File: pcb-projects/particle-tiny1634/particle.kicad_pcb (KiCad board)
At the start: 2 copper layers, 16 parts, among them IC1 ATTINY1634-SU, P1 CONN_02X03, P2 CONN_02X03

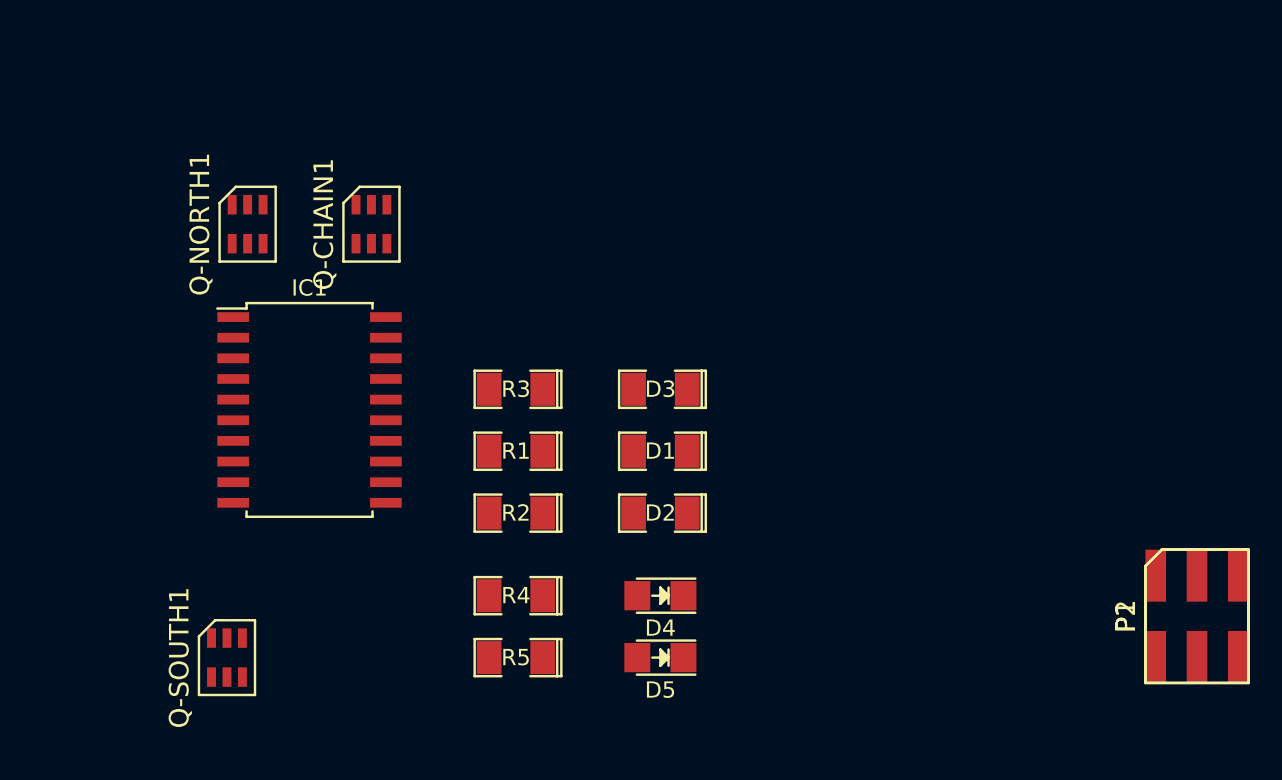
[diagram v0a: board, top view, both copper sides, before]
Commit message: routed attiny1634 particle
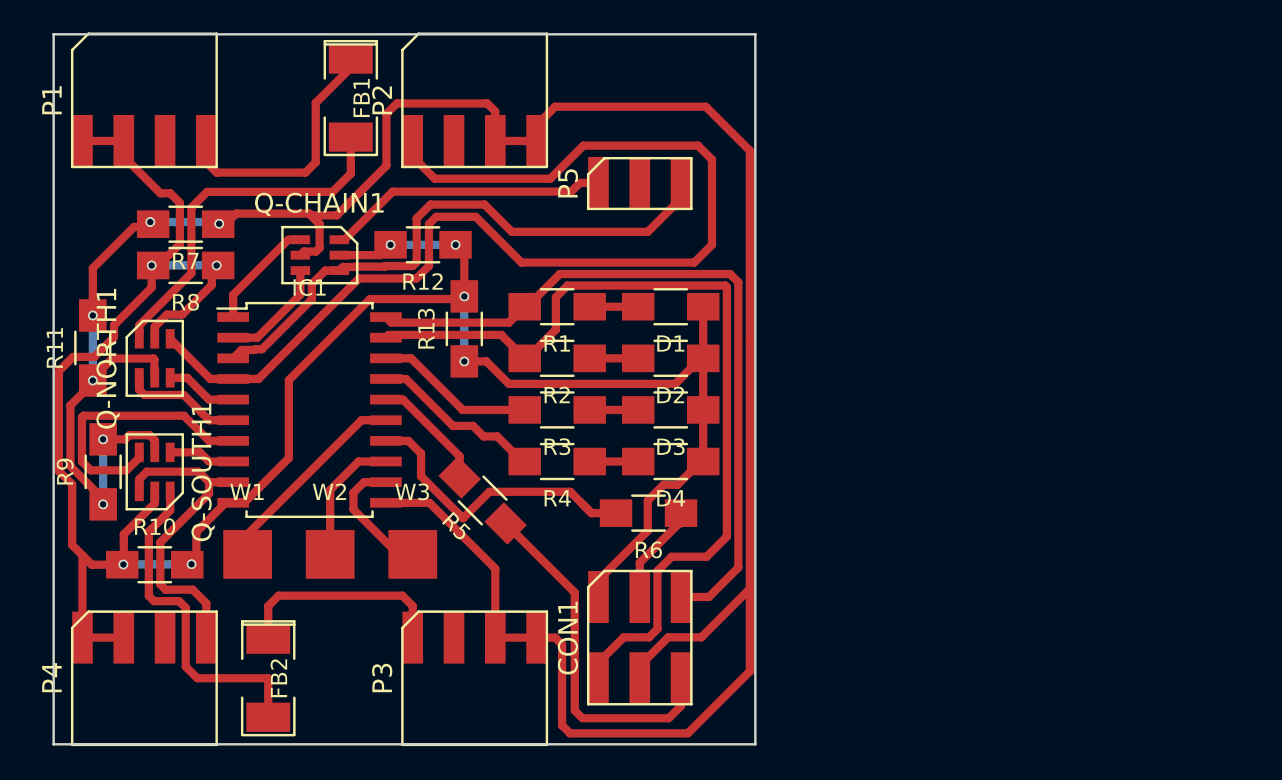
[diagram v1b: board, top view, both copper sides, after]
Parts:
- removed D5: LED, LEDs:LED-1206
- added CON1: AVR-ISP-6, SMT_PIN_HEADER:CONN-6, F.Cu at (170.2, 122.0)
- added FB1: TX-SMA-N, SMD_Packages:SMD-2010_Pol, F.Cu at (152.4, 88.8)
- added FB2: TX-SMA-S, SMD_Packages:SMD-2010_Pol, F.Cu at (147.3, 124.5)
- added P3: TXS, SMT_PIN_HEADER:CONN-8_5-8, F.Cu at (160.0, 124.5)
- added P4: RXS, SMT_PIN_HEADER:CONN-8_5-8, F.Cu at (139.7, 124.5)
- added P5: TRXCH, SMT_PIN_HEADER:CONN-1x3, F.Cu at (170.2, 94.0)
- added R10: 0, Resistors_SMD:R_1206_HandSoldering, F.Cu at (140.3, 117.5)
- added R11: 0, Resistors_SMD:R_1206_HandSoldering, F.Cu at (136.5, 104.1)
- added R12: 0, Resistors_SMD:R_1206_HandSoldering, F.Cu at (156.8, 97.8)
- added R13: 0, Resistors_SMD:R_1206_HandSoldering, F.Cu at (159.4, 103.0)
- added R6: 0, Resistors_SMD:R_1206_HandSoldering, F.Cu at (170.7, 114.3)
- added R7: 0, Resistors_SMD:R_1206_HandSoldering, F.Cu at (142.2, 96.5)
- added R8: 0, Resistors_SMD:R_1206_HandSoldering, F.Cu at (142.2, 99.1)
- added R9: 0, Resistors_SMD:R_1206_HandSoldering, F.Cu at (137.2, 111.8)
- added W1: TEST_1P, Measurement_Points:Measurement_Point_Square-SMD-Pad_Big, F.Cu at (146.1, 116.8)
- added W2: TEST_1P, Measurement_Points:Measurement_Point_Square-SMD-Pad_Big, F.Cu at (151.1, 116.8)
- added W3: TEST_1P, Measurement_Points:Measurement_Point_Square-SMD-Pad_Big, F.Cu at (156.2, 116.8)
- D1: value LED -> HB; footprint SMD_Packages:SMD-1206_Pol -> Resistors_SMD:R_1206_HandSoldering
- D2: value LED -> STATUS0; footprint SMD_Packages:SMD-1206_Pol -> Resistors_SMD:R_1206_HandSoldering
- D3: value LED -> STATUS1; footprint SMD_Packages:SMD-1206_Pol -> Resistors_SMD:R_1206_HandSoldering
- D4: value LED -> ERROR; footprint LEDs:LED-1206 -> Resistors_SMD:R_1206_HandSoldering
- P1: value CONN_02X03 -> TXN; footprint SMT_PIN_HEADER:CONN-6_1-3 -> SMT_PIN_HEADER:CONN-8_1-4
- P2: value CONN_02X03 -> RXN; footprint SMT_PIN_HEADER:CONN-6_4-6 -> SMT_PIN_HEADER:CONN-8_1-4
- R1, R2, R3, R4: value R_Small -> 1k2; footprint SMD_Packages:SMD-1206_Pol -> Resistors_SMD:R_1206_HandSoldering
- R5: value R_Small -> 0; footprint SMD_Packages:SMD-1206_Pol -> Resistors_SMD:R_1206_HandSoldering
- moved P1 72.1 mm to (139.7, 88.9)
- moved P2 54.6 mm to (160.0, 88.9)
- moved Q-SOUTH1 12.3 mm to (140.3, 111.8), turned to 180 degrees
- moved Q-NORTH1 10.0 mm to (140.3, 104.8)
- moved R5 9.88 mm to (160.5, 113.5), turned to 135 degrees
- moved R2 9.86 mm to (165.1, 104.8)
- moved D2 9.55 mm to (172.1, 104.8)
- moved R1 9.25 mm to (165.1, 101.6)
- moved D1 8.91 mm to (172.1, 101.6)
- moved R4 8.64 mm to (165.1, 111.1)
- moved D4 8.28 mm to (172.1, 111.1)
- moved Q-CHAIN1 3.70 mm to (150.5, 98.4), turned to 270 degrees
- moved R3 2.84 mm to (165.1, 108.0)
- moved D3 1.42 mm to (172.1, 108.0)
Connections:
- D1 pad 1: VCC -> GND
- D2 pad 1: VCC -> GND
- D3 pad 1: VCC -> GND
- D4 pad 1: VCC -> GND
- IC1 pad 1: (no net) -> /PWR/TX-CHAIN
- IC1 pad 10: (no net) -> GND
- IC1 pad 12: (no net) -> /TP3
- IC1 pad 13: (no net) -> /TP2
- IC1 pad 14: (no net) -> Net-(IC1-Pad14)
- IC1 pad 15: (no net) -> /TP1
- IC1 pad 16: (no net) -> Net-(IC1-Pad16)
- IC1 pad 17: (no net) -> /ERROR
- IC1 pad 18: (no net) -> /STATUS1
- IC1 pad 19: (no net) -> /MISO
- IC1 pad 2: (no net) -> /SW_PWR/RX-CHAIN
- IC1 pad 20: (no net) -> /MOSI
- IC1 pad 3: (no net) -> /RX-CHAIN
- IC1 pad 4: (no net) -> /RX-NORTH
- IC1 pad 5: (no net) -> /SW_PWR/RX-NORTH
- IC1 pad 6: (no net) -> /PWR/TX-NORTH
- IC1 pad 7: (no net) -> /SW_PWR/RX-SOUTH
- IC1 pad 8: (no net) -> /PWR/TX-SOUTH
- IC1 pad 9: (no net) -> /RX-SOUTH
- P1 pad 1: (no net) -> GND
- P1 pad 2: (no net) -> GND
- P2 pad 4: (no net) -> VCC
- Q-CHAIN1 pad 1: (no net) -> /PWR/TX-CHAIN
- Q-CHAIN1 pad 3: (no net) -> /SW_PWR/RX-CHAIN
- Q-CHAIN1 pad 4: (no net) -> /RX-CHAIN
- Q-NORTH1 pad 1: (no net) -> /PWR/TX-NORTH
- Q-NORTH1 pad 3: (no net) -> /SW_PWR/RX-NORTH
- Q-NORTH1 pad 4: (no net) -> /RX-NORTH
- Q-NORTH1 pad 6: /TX-NORTH -> Net-(FB1-Pad2)
- Q-SOUTH1 pad 1: (no net) -> /PWR/TX-SOUTH
- Q-SOUTH1 pad 3: (no net) -> /SW_PWR/RX-SOUTH
- Q-SOUTH1 pad 4: (no net) -> /RX-SOUTH
- Q-SOUTH1 pad 6: /TX-SOUTH -> Net-(FB2-Pad2)
- R1 pad 2: /TX-SOUTH -> /MOSI
- R2 pad 2: /TX-NORTH -> /MISO
- R3 pad 2: /TX-CHAIN -> /STATUS1
- R4 pad 2: (no net) -> /ERROR
- R5 pad 1: Net-(D5-Pad2) -> /SCK
- R5 pad 2: (no net) -> Net-(IC1-Pad16)
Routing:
- net VCC: track 0.00 -> 162.6 mm, vias 0 -> 6
- net GND: track 0.00 -> 144.3 mm, vias 0 -> 8
- net /RX-NORTH: track 0.00 -> 68.8 mm
- net /MISO: track 0.00 -> 54.2 mm
- net /MOSI: track 0.00 -> 45.1 mm
- net /RX-CHAIN: track 0.00 -> 36.1 mm
- net Net-(FB1-Pad2): track 0.00 -> 22.0 mm
- net /SCK: track 0.00 -> 21.9 mm
- net /RX-SOUTH: track 0.00 -> 21.3 mm
- net Net-(FB2-Pad2): track 0.00 -> 20.9 mm
- net Net-(IC1-Pad14): track 0.00 -> 19.0 mm
- net /TX-CHAIN: track 0.00 -> 17.4 mm
- net /SW_PWR/RX-SOUTH: track 0.00 -> 17.1 mm
- net /TX-NORTH: track 0.00 -> 15.8 mm
- net /TX-SOUTH: track 0.00 -> 13.4 mm
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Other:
- board outline added: 43.2 x 43.7 mm
- net class Default: trace_width 0.25 -> 0.508

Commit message: cosmetics
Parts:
- moved P5 2.26 mm to (171.4, 95.9)
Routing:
- net VCC: track 162.6 -> 159.3 mm
- net /RX-CHAIN: track 36.1 -> 38.2 mm
- net /TX-CHAIN: track 17.4 -> 19.0 mm
- net /RX-NORTH: track 68.8 -> 69.4 mm
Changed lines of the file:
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@@
     (links 68)
     (no_connects 0)
-    (area 134.036999 84.758046 177.367001 128.599185)
+    (area 132.66 84.390062 177.409025 128.835001)
     (thickness 1.6)
     (drawings 4)
-    (tracks 341)
+    (tracks 340)
     (zones 0)
     (modules 32)
@@
   )
   (module SMT_PIN_HEADER:CONN-1x3 (layer F.Cu)
-    (at 170.18 94.02)
+    (at 171.45 95.885)
     (fp_text reference P5 (at -4.375 0 90) (layer F.SilkS)
       (effects (font (size 1.2 1.2) (thickness 0.15)))
@@
   (segment (start 174.085 104.775) (end 174.085 107.95) (width 0.508) (layer F.Cu) (net 1) (status 30))
   (segment (start 174.085 101.6) (end 174.085 104.775) (width 0.508) (layer F.Cu) (net 1) (status 30))
+  (segment (start 176.955023 118.954977) (end 176.955023 103.52178) (width 0.508) (layer F.Cu) (net 2))
+  (segment (start 164.989183 92.559183) (end 163.83 91.4) (width 0.508) (layer F.Cu) (net 2))
+  (segment (start 176.955023 103.52178) (end 176.955021 103.521778) (width 0.508) (layer F.Cu) (net 2))
+  (segment (start 176.955021 103.521778) (end 176.955021 93.809474) (width 0.508) (layer F.Cu) (net 2))
+  (segment (start 175.70473 92.559183) (end 164.989183 92.559183) (width 0.508) (layer F.Cu) (net 2))
+  (segment (start 176.955021 93.809474) (end 175.70473 92.559183) (width 0.508) (layer F.Cu) (net 2))
   (segment (start 154.56 113.665) (end 157.237818 113.665) (width 0.508) (layer F.Cu) (net 2))
   (segment (start 157.237818 113.665) (end 161.29 117.717182) (width 0.508) (layer F.Cu) (net 2))
@@
   (segment (start 149.956803 95.978392) (end 150.477649 96.499238) (width 0.508) (layer F.Cu) (net 2))
   (segment (start 163.83 91.4) (end 161.29 91.4) (width 0.508) (layer F.Cu) (net 2))
-  (segment (start 176.955023 118.954977) (end 176.955023 103.52178) (width 0.508) (layer F.Cu) (net 2))
-  (segment (start 176.955023 103.52178) (end 176.955021 103.521778) (width 0.508) (layer F.Cu) (net 2))
-  (segment (start 176.955021 103.521778) (end 176.955021 91.998596) (width 0.508) (layer F.Cu) (net 2))
-  (segment (start 176.955021 91.998596) (end 174.248425 89.292) (width 0.508) (layer F.Cu) (net 2))
-  (segment (start 174.248425 89.292) (end 164.973 89.292) (width 0.508) (layer F.Cu) (net 2))
-  (segment (start 164.973 89.292) (end 163.83 90.435) (width 0.508) (layer F.Cu) (net 2))
-  (segment (start 163.83 90.435) (end 163.83 91.4) (width 0.508) (layer F.Cu) (net 2))
   (segment (start 176.955023 118.954977) (end 173.96955 121.94045) (width 0.508) (layer F.Cu) (net 2))
   (segment (start 173.96955 121.94045) (end 171.932659 121.94045) (width 0.508) (layer F.Cu) (net 2))
@@
   (segment (start 143.677 107.315) (end 142.337 105.975) (width 0.508) (layer F.Cu) (net 13))
   (segment (start 142.337 105.975) (end 141.285 105.975) (width 0.508) (layer F.Cu) (net 13) (status 20))
-  (segment (start 166.711298 91.688027) (end 164.676686 93.722639) (width 0.508) (layer F.Cu) (net 14))
+  (segment (start 175.488541 93.409214) (end 166.524393 93.409214) (width 0.508) (layer F.Cu) (net 14))
+  (segment (start 157.654118 96.066858) (end 160.087973 96.066858) (width 0.508) (layer F.Cu) (net 14))
   (segment (start 145.16 106.045) (end 146.717202 106.045) (width 0.508) (layer F.Cu) (net 14))
+  (segment (start 157.209066 96.51191) (end 157.654118 96.066858) (width 0.508) (layer F.Cu) (net 14))
+  (segment (start 146.717202 106.045) (end 152.90019 99.862012) (width 0.508) (layer F.Cu) (net 14))
+  (segment (start 166.524393 93.409214) (end 166.210968 93.722639) (width 0.508) (layer F.Cu) (net 14))
+  (segment (start 174.909139 98.879977) (end 176.016408 97.772708) (width 0.508) (layer F.Cu) (net 14))
+  (segment (start 152.90019 99.862012) (end 156.441468 99.862012) (width 0.508) (layer F.Cu) (net 14))
   (segment (start 156.441468 99.862012) (end 157.209066 99.094414) (width 0.508) (layer F.Cu) (net 14))
-  (segment (start 146.717202 106.045) (end 152.90019 99.862012) (width 0.508) (layer F.Cu) (net 14))
-  (segment (start 152.90019 99.862012) (end 156.441468 99.862012) (width 0.508) (layer F.Cu) (net 14))
-  (segment (start 174.625 92.545673) (end 173.767354 91.688027) (width 0.508) (layer F.Cu) (net 14))
   (segment (start 157.209066 99.094414) (end 157.209066 96.51191) (width 0.508) (layer F.Cu) (net 14))
-  (segment (start 157.209066 96.51191) (end 157.654118 96.066858) (width 0.508) (layer F.Cu) (net 14))
-  (segment (start 173.767354 91.688027) (end 166.711298 91.688027) (width 0.508) (layer F.Cu) (net 14))
   (segment (start 157.567639 93.722639) (end 156.21 92.365) (width 0.508) (layer F.Cu) (net 14))
-  (segment (start 173.535023 98.879977) (end 174.625 97.79) (width 0.508) (layer F.Cu) (net 14))
-  (segment (start 157.654118 96.066858) (end 160.087973 96.066858) (width 0.508) (layer F.Cu) (net 14))
-  (segment (start 164.676686 93.722639) (end 157.567639 93.722639) (width 0.508) (layer F.Cu) (net 14))
   (segment (start 160.087973 96.066858) (end 162.901092 98.879977) (width 0.508) (layer F.Cu) (net 14))
-  (segment (start 162.901092 98.879977) (end 173.535023 98.879977) (width 0.508) (layer F.Cu) (net 14))
-  (segment (start 174.625 97.79) (end 174.625 92.545673) (width 0.508) (layer F.Cu) (net 14))
+  (segment (start 162.901092 98.879977) (end 174.909139 98.879977) (width 0.508) (layer F.Cu) (net 14))
+  (segment (start 176.016408 97.772708) (end 176.016408 93.937081) (width 0.508) (layer F.Cu) (net 14))
+  (segment (start 176.016408 93.937081) (end 175.488541 93.409214) (width 0.508) (layer F.Cu) (net 14))
+  (segment (start 166.210968 93.722639) (end 157.567639 93.722639) (width 0.508) (layer F.Cu) (net 14))
   (segment (start 156.21 92.365) (end 156.21 91.4) (width 0.508) (layer F.Cu) (net 14))
   (segment (start 145.16 106.045) (end 143.755 106.045) (width 0.508) (layer F.Cu) (net 14) (status 10))
@@
   (segment (start 149.295 100.853) (end 149.295 99.375) (width 0.508) (layer F.Cu) (net 16) (status 20))
   (segment (start 151.695 99.375) (end 151.915999 99.154001) (width 0.508) (layer F.Cu) (net 17))
+  (segment (start 151.915999 99.154001) (end 152.658201 99.154001) (width 0.508) (layer F.Cu) (net 17))
+  (segment (start 156.208201 99.094001) (end 156.452564 98.849638) (width 0.508) (layer F.Cu) (net 17))
+  (segment (start 152.658201 99.154001) (end 152.679192 99.13301) (width 0.508) (layer F.Cu) (net 17))
+  (segment (start 154.542276 99.094001) (end 156.208201 99.094001) (width 0.508) (layer F.Cu) (net 17))
+  (segment (start 152.679192 99.13301) (end 154.503267 99.13301) (width 0.508) (layer F.Cu) (net 17))
+  (segment (start 154.503267 99.13301) (end 154.542276 99.094001) (width 0.508) (layer F.Cu) (net 17))
   (segment (start 156.452564 98.849638) (end 156.452564 96.16217) (width 0.508) (layer F.Cu) (net 17))
+  (segment (start 163.430507 98.11272) (end 173.83028 98.11272) (width 0.508) (layer F.Cu) (net 17))
   (segment (start 156.452564 96.16217) (end 157.301558 95.313176) (width 0.508) (layer F.Cu) (net 17))
-  (segment (start 151.915999 99.154001) (end 152.658201 99.154001) (width 0.508) (layer F.Cu) (net 17))
-  (segment (start 152.679192 99.13301) (end 154.503267 99.13301) (width 0.508) (layer F.Cu) (net 17))
-  (segment (start 152.658201 99.154001) (end 152.679192 99.13301) (width 0.508) (layer F.Cu) (net 17))
-  (segment (start 156.208201 99.094001) (end 156.452564 98.849638) (width 0.508) (layer F.Cu) (net 17))
-  (segment (start 154.503267 99.13301) (end 154.542276 99.094001) (width 0.508) (layer F.Cu) (net 17))
-  (segment (start 154.542276 99.094001) (end 156.208201 99.094001) (width 0.508) (layer F.Cu) (net 17))
+  (segment (start 160.630963 95.313176) (end 163.430507 98.11272) (width 0.508) (layer F.Cu) (net 17))
   (segment (start 157.301558 95.313176) (end 160.630963 95.313176) (width 0.508) (layer F.Cu) (net 17))
-  (segment (start 160.630963 95.313176) (end 162.307571 96.989784) (width 0.508) (layer F.Cu) (net 17))
-  (segment (start 162.307571 96.989784) (end 170.675216 96.989784) (width 0.508) (layer F.Cu) (net 17))
-  (segment (start 170.675216 96.989784) (end 172.72 94.945) (width 0.508) (layer F.Cu) (net 17))
-  (segment (start 172.72 94.945) (end 172.72 93.98) (width 0.508) (layer F.Cu) (net 17))
+  (segment (start 173.83028 98.11272) (end 173.99 97.953) (width 0.508) (layer F.Cu) (net 17))
+  (segment (start 173.99 97.953) (end 173.99 95.845) (width 0.508) (layer F.Cu) (net 17))
   (segment (start 150.00301 101.146267) (end 150.00301 100.20071) (width 0.508) (layer F.Cu) (net 17))
   (segment (start 145.675999 104.259001) (end 146.498201 104.259001) (width 0.508) (layer F.Cu) (net 17))
@@
   (segment (start 159.282816 107.95) (end 163.1 107.95) (width 0.508) (layer F.Cu) (net 21) (status 20))
   (segment (start 151.695 97.475) (end 152.02 97.475) (width 0.508) (layer F.Cu) (net 22))
+  (segment (start 161.229519 94.517908) (end 162.556611 95.845) (width 0.508) (layer F.Cu) (net 22))
   (segment (start 152.02 97.475) (end 154.977092 94.517908) (width 0.508) (layer F.Cu) (net 22))
-  (segment (start 154.977092 94.517908) (end 165.959092 94.517908) (width 0.508) (layer F.Cu) (net 22))
-  (segment (start 165.959092 94.517908) (end 166.497 93.98) (width 0.508) (layer F.Cu) (net 22))
-  (segment (start 166.497 93.98) (end 167.64 93.98) (width 0.508) (layer F.Cu) (net 22))
+  (segment (start 154.977092 94.517908) (end 161.229519 94.517908) (width 0.508) (layer F.Cu) (net 22))
+  (segment (start 162.556611 95.845) (end 168.91 95.845) (width 0.508) (layer F.Cu) (net 22))
   (segment (start 143.51 91.4) (end 143.51 92.71) (width 0.508) (layer F.Cu) (net 23))
   (segment (start 150.241321 89.059369) (end 152.4 86.90069) (width 0.508) (layer F.Cu) (net 23))

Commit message: cosmetics
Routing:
- net VCC: track 159.3 -> 160.0 mm
